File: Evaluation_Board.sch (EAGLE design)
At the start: 38 parts, among them IC1 MEGA32-A, IC2 FT232RL, IC3 317EMP, J1 DCJ0202, Q1 16 MHz

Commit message: Port A beschriftet
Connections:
- net N$10 renamed A3
- net N$11 renamed A2
- net N$12 renamed A1
- net N$13 renamed A0
- net N$6 renamed A7
- net N$7 renamed A6
- net N$8 renamed A5
- net N$9 renamed A4
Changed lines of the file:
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@@
 <?xml version="1.0" encoding="utf-8"?>
 <!DOCTYPE eagle SYSTEM "eagle.dtd">
-<eagle version="6.5.0">
+<eagle version="6.4">
 <drawing>
 <settings>
@@
 </segment>
 </net>
-<net name="N$6" class="0">
+<net name="A7" class="0">
 <segment>
 <pinref part="IC1" gate="G$1" pin="(ADC7)PA7"/>
@@
 </segment>
 </net>
-<net name="N$7" class="0">
+<net name="A6" class="0">
 <segment>
 <pinref part="IC1" gate="G$1" pin="(ADC6)PA6"/>
@@
 </segment>
 </net>
-<net name="N$8" class="0">
+<net name="A5" class="0">
 <segment>
 <pinref part="SV2" gate="A" pin="3"/>
@@
 </segment>
 </net>
-<net name="N$9" class="0">
+<net name="A4" class="0">
 <segment>
 <pinref part="IC1" gate="G$1" pin="(ADC4)PA4"/>
@@
 </segment>
 </net>
-<net name="N$10" class="0">
+<net name="A3" class="0">
 <segment>
 <pinref part="IC1" gate="G$1" pin="(ADC3)PA3"/>
@@
 </segment>
 </net>
-<net name="N$11" class="0">
+<net name="A2" class="0">
 <segment>
 <pinref part="IC1" gate="G$1" pin="(ADC2)PA2"/>
@@
 </segment>
 </net>
-<net name="N$12" class="0">
+<net name="A1" class="0">
 <segment>
 <pinref part="IC1" gate="G$1" pin="(ADC1)PA1"/>
@@
 </segment>
 </net>
-<net name="N$13" class="0">
+<net name="A0" class="0">
 <segment>
 <pinref part="IC1" gate="G$1" pin="(ADC0)PA0"/>

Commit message: Alle Beschriftungen eingefuegt
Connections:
- net N$31 renamed C2
- net N$32 renamed C3
- net N$33 renamed C4
- net N$34 renamed C5
- net N$35 renamed C6
- net N$36 renamed C7
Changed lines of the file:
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@@
 </segment>
 </net>
-<net name="N$31" class="0">
+<net name="C2" class="0">
 <segment>
 <pinref part="IC1" gate="G$1" pin="(TCK)PC2"/>
@@
 </segment>
 </net>
-<net name="N$32" class="0">
+<net name="C3" class="0">
 <segment>
 <pinref part="IC1" gate="G$1" pin="(TMS)PC3"/>
@@
 </segment>
 </net>
-<net name="N$33" class="0">
+<net name="C4" class="0">
 <segment>
 <pinref part="IC1" gate="G$1" pin="(TDO)PC4"/>
@@
 </segment>
 </net>
-<net name="N$34" class="0">
+<net name="C5" class="0">
 <segment>
 <pinref part="IC1" gate="G$1" pin="(TDI)PC5"/>
@@
 </segment>
 </net>
-<net name="N$35" class="0">
+<net name="C6" class="0">
 <segment>
 <pinref part="IC1" gate="G$1" pin="(TOSC1)PC6"/>
@@
 </segment>
 </net>
-<net name="N$36" class="0">
+<net name="C7" class="0">
 <segment>
 <pinref part="IC1" gate="G$1" pin="(TOSC2)PC7"/>

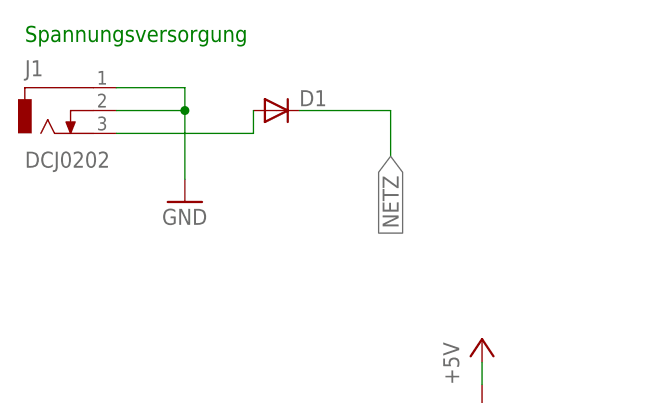
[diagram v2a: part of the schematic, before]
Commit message: DC Jack geaendert
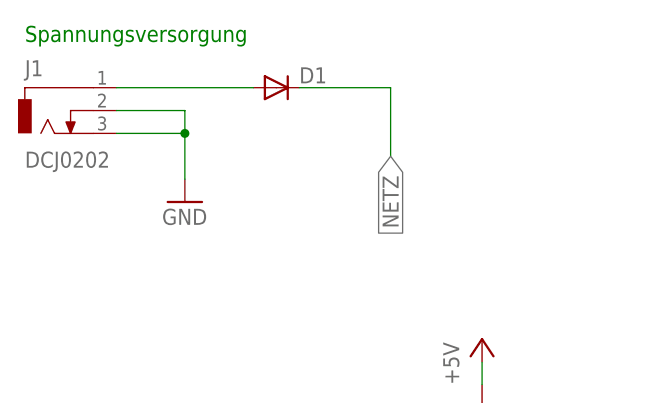
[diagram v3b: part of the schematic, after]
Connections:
- removed net N$3: D1.A, J1.3
- new net N$2: D1.A, J1.1
- net GND: now also J1.3; no longer J1.1
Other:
- moved on the sheet: D1
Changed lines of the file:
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@@
 <instance part="J1" gate="G$1" x="30.48" y="243.84"/>
 <instance part="SUPPLY6" gate="1" x="45.72" y="233.68"/>
-<instance part="D1" gate="G$1" x="55.88" y="243.84"/>
+<instance part="D1" gate="G$1" x="55.88" y="246.38"/>
 <instance part="LED1" gate="G$1" x="281.94" y="223.52" rot="R90"/>
 <instance part="SUPPLY10" gate="1" x="292.1" y="223.52" rot="R90"/>
@@
 <segment>
 <pinref part="D1" gate="G$1" pin="C"/>
-<wire x1="58.42" y1="243.84" x2="68.58" y2="243.84" width="0.1524" layer="91"/>
-<wire x1="68.58" y1="243.84" x2="68.58" y2="238.76" width="0.1524" layer="91"/>
+<wire x1="58.42" y1="246.38" x2="68.58" y2="246.38" width="0.1524" layer="91"/>
+<wire x1="68.58" y1="246.38" x2="68.58" y2="238.76" width="0.1524" layer="91"/>
 <label x="68.58" y="238.76" size="1.778" layer="95" rot="R270" xref="yes"/>
 </segment>
@@
 </segment>
 <segment>
-<pinref part="J1" gate="G$1" pin="1"/>
-<wire x1="38.1" y1="246.38" x2="45.72" y2="246.38" width="0.1524" layer="91"/>
-<pinref part="SUPPLY6" gate="1" pin="GND"/>
-<wire x1="45.72" y1="236.22" x2="45.72" y2="243.84" width="0.1524" layer="91"/>
-<pinref part="J1" gate="G$1" pin="2"/>
-<wire x1="45.72" y1="243.84" x2="45.72" y2="246.38" width="0.1524" layer="91"/>
-<wire x1="38.1" y1="243.84" x2="45.72" y2="243.84" width="0.1524" layer="91"/>
-<junction x="45.72" y="243.84"/>
-</segment>
-<segment>
 <pinref part="S3" gate="1" pin="P"/>
 <pinref part="S3" gate="1" pin="P1"/>
@@
 <wire x1="60.96" y1="187.96" x2="63.5" y2="187.96" width="0.1524" layer="91"/>
 <junction x="63.5" y="187.96"/>
+</segment>
+<segment>
+<pinref part="J1" gate="G$1" pin="2"/>
+<wire x1="38.1" y1="243.84" x2="45.72" y2="243.84" width="0.1524" layer="91"/>
+<pinref part="SUPPLY6" gate="1" pin="GND"/>
+<wire x1="45.72" y1="243.84" x2="45.72" y2="241.3" width="0.1524" layer="91"/>
+<pinref part="J1" gate="G$1" pin="3"/>
+<wire x1="45.72" y1="241.3" x2="45.72" y2="236.22" width="0.1524" layer="91"/>
+<wire x1="38.1" y1="241.3" x2="45.72" y2="241.3" width="0.1524" layer="91"/>
+<junction x="45.72" y="241.3"/>
 </segment>
 </net>
@@
 </segment>
 </net>
-<net name="N$3" class="0">
-<segment>
-<pinref part="J1" gate="G$1" pin="3"/>
-<pinref part="D1" gate="G$1" pin="A"/>
-<wire x1="38.1" y1="241.3" x2="53.34" y2="241.3" width="0.1524" layer="91"/>
-<wire x1="53.34" y1="241.3" x2="53.34" y2="243.84" width="0.1524" layer="91"/>
-</segment>
-</net>
 <net name="N$1" class="0">
 <segment>
@@
 </segment>
 </net>
+<net name="N$2" class="0">
+<segment>
+<pinref part="J1" gate="G$1" pin="1"/>
+<wire x1="38.1" y1="246.38" x2="53.34" y2="246.38" width="0.1524" layer="91"/>
+<pinref part="D1" gate="G$1" pin="A"/>
+</segment>
+</net>
